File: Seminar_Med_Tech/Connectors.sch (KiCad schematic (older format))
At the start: 12 parts, among them J1 TP10, J2 CONN_02X10, J3 TP7, J4 CONN_02X10

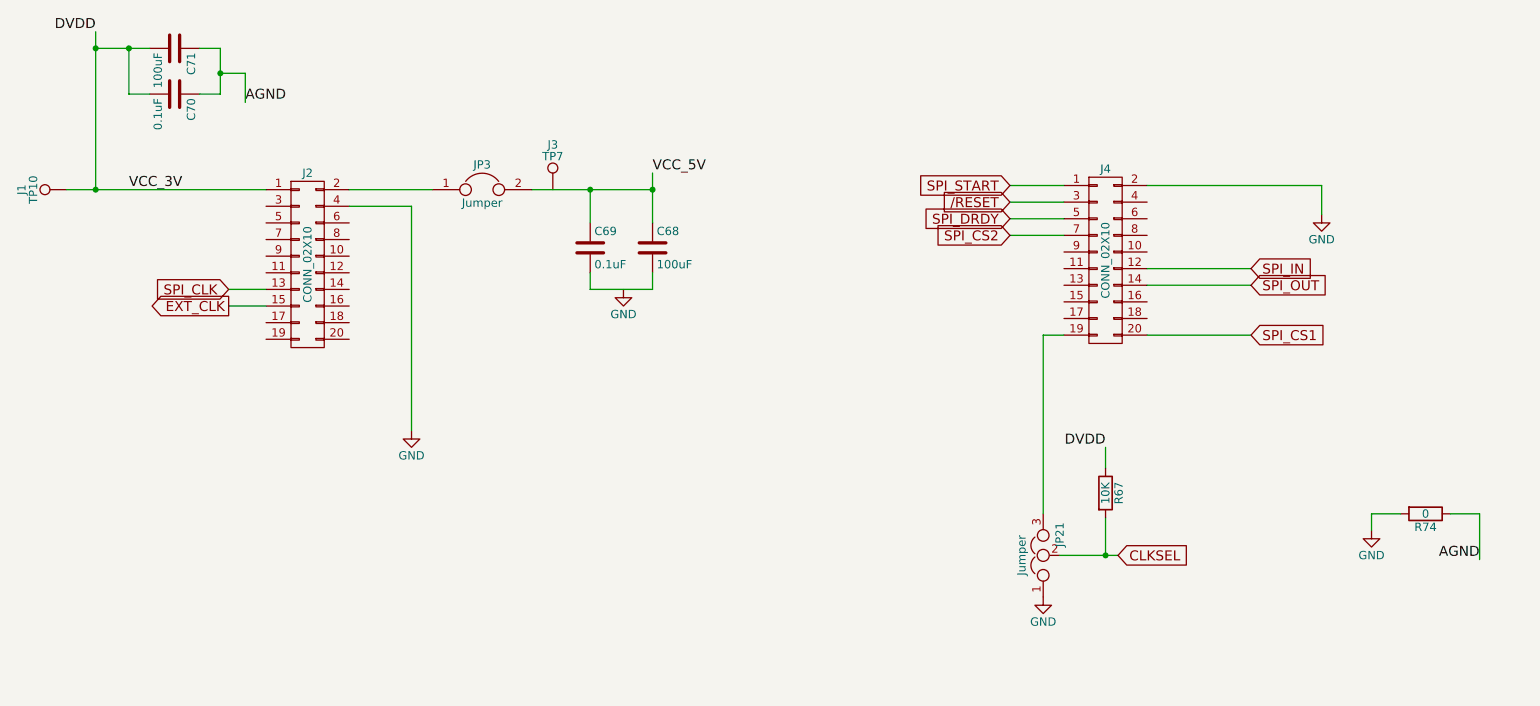
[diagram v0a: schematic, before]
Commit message: Changed labels in ADC1298_ECG_FE
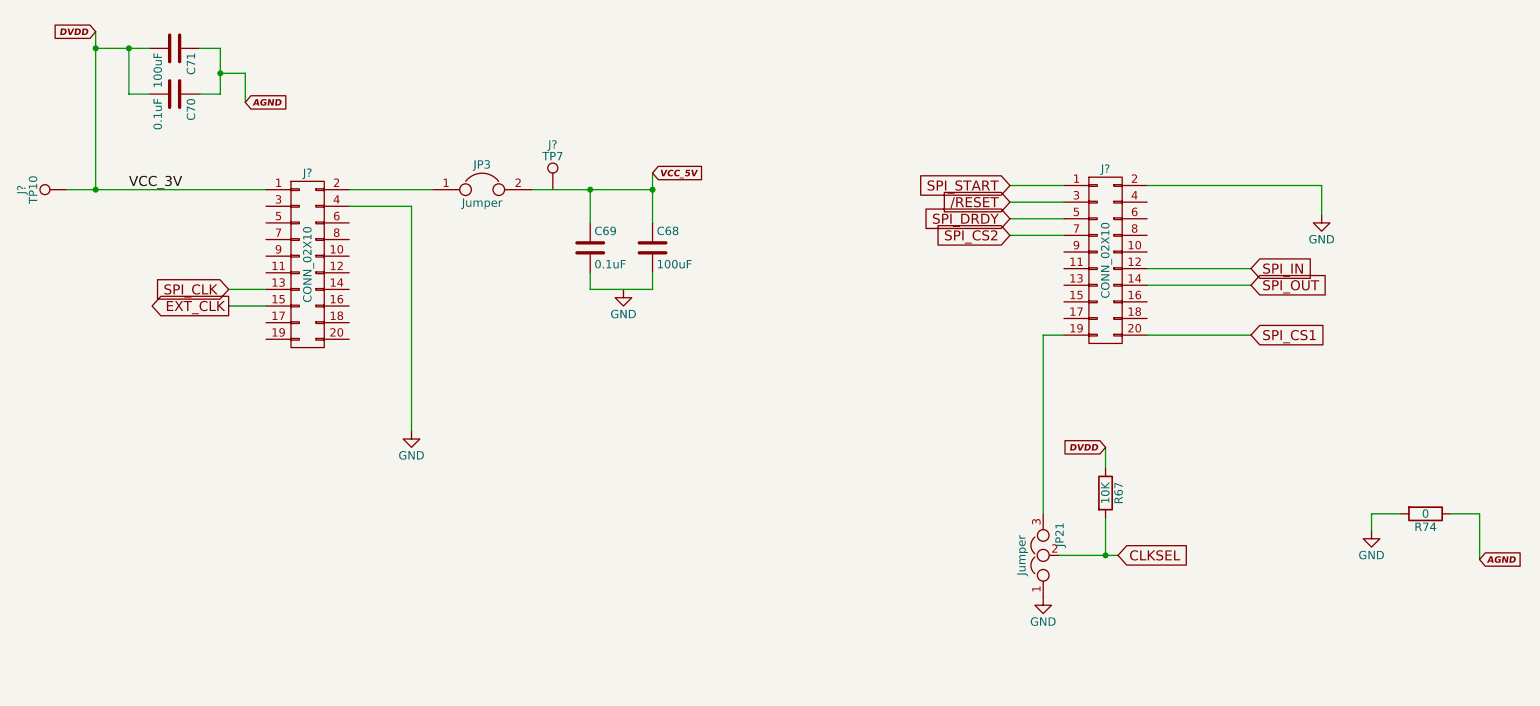
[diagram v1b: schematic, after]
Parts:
- C68, C69, C70, C71: footprint Capacitors_SMD:C_1206_HandSoldering -> (none)
- J?: renamed from J2; footprint Pin_Headers:Pin_Header_Angled_2x10_Pitch2.54mm -> (none)
- J?: renamed from J4; footprint Pin_Headers:Pin_Header_Angled_2x10_Pitch2.54mm -> (none)
- J?: renamed from J1; footprint Measurement_Points:Test_Point -> (none)
- J?: renamed from J3; footprint Measurement_Points:Test_Point -> (none)
- JP21: footprint jumper:jumper1x3 -> (none)
- JP3: footprint jumper:Jumper1x2 -> (none)
- R67, R74: footprint Resistors_SMD:R_0805_HandSoldering -> (none)
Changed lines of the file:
@@
 $EndDescr
 $Comp
-L CONN_02X10 J2
+L CONN_02X10 J?
 U 1 1 593ACF11
 P 2800 4000
-F 0 "J2" H 2800 4550 50  0000 C CNN
+F 0 "J?" H 2800 4550 50  0000 C CNN
 F 1 "CONN_02X10" V 2800 4000 50  0000 C CNN
-F 2 "Pin_Headers:Pin_Header_Angled_2x10_Pitch2.54mm" H 2800 2800 50  0001 C CNN
+F 2 "" H 2800 2800 50  0001 C CNN
 F 3 "" H 2800 2800 50  0001 C CNN
 	1    2800 4000
@@
 $EndComp
 $Comp
-L CONN_02X10 J4
+L CONN_02X10 J?
 U 1 1 593AD152
 P 7600 3975
-F 0 "J4" H 7600 4525 50  0000 C CNN
+F 0 "J?" H 7600 4525 50  0000 C CNN
 F 1 "CONN_02X10" V 7600 3975 50  0000 C CNN
-F 2 "Pin_Headers:Pin_Header_Angled_2x10_Pitch2.54mm" H 7600 2775 50  0001 C CNN
+F 2 "" H 7600 2775 50  0001 C CNN
 F 3 "" H 7600 2775 50  0001 C CNN
 	1    7600 3975
@@
 F 0 "JP21" H 7275 5650 50  0000 L CNN
 F 1 "Jumper" H 7225 5850 50  0000 C BNN
-F 2 "jumper:jumper1x3" H 7225 5750 50  0001 C CNN
+F 2 "" H 7225 5750 50  0001 C CNN
 F 3 "" H 7225 5750 50  0001 C CNN
 	1    7225 5750
@@
 F 0 "R67" V 7680 5375 50  0000 C CNN
 F 1 "10K" V 7600 5375 50  0000 C CNN
-F 2 "Resistors_SMD:R_0805_HandSoldering" V 7530 5375 50  0001 C CNN
+F 2 "" V 7530 5375 50  0001 C CNN
 F 3 "" H 7600 5375 50  0001 C CNN
 	1    7600 5375
 	1    0    0    -1
 $EndComp
-Text Label 7600 5100 2    60   ~ 0
-DVDD
-$Comp
-L GND #PWR01
+$Comp
+L GND #PWR?
 U 1 1 593AE084
 P 7225 6000
-F 0 "#PWR01" H 7225 5750 50  0001 C CNN
+F 0 "#PWR?" H 7225 5750 50  0001 C CNN
 F 1 "GND" H 7225 5850 50  0000 C CNN
 F 2 "" H 7225 6000 50  0001 C CNN
@@
 $EndComp
 $Comp
-L GND #PWR02
+L GND #PWR?
 U 1 1 593AE114
 P 3425 5000
-F 0 "#PWR02" H 3425 4750 50  0001 C CNN
+F 0 "#PWR?" H 3425 4750 50  0001 C CNN
 F 1 "GND" H 3425 4850 50  0000 C CNN
 F 2 "" H 3425 5000 50  0001 C CNN
@@
 $EndComp
 $Comp
-L GND #PWR03
+L GND #PWR?
 U 1 1 593AE149
 P 8900 3700
-F 0 "#PWR03" H 8900 3450 50  0001 C CNN
+F 0 "#PWR?" H 8900 3450 50  0001 C CNN
 F 1 "GND" H 8900 3550 50  0000 C CNN
 F 2 "" H 8900 3700 50  0001 C CNN
@@
 SPI_CS1
 $Comp
-L GND #PWR04
+L GND #PWR?
 U 1 1 593E72B3
 P 9200 5600
-F 0 "#PWR04" H 9200 5350 50  0001 C CNN
+F 0 "#PWR?" H 9200 5350 50  0001 C CNN
 F 1 "GND" H 9200 5450 50  0000 C CNN
 F 2 "" H 9200 5600 50  0001 C CNN
@@
 F 0 "R74" V 9605 5500 50  0000 C CNN
 F 1 "0" V 9525 5500 50  0000 C CNN
-F 2 "Resistors_SMD:R_0805_HandSoldering" V 9455 5500 50  0001 C CNN
+F 2 "" V 9455 5500 50  0001 C CNN
 F 3 "" H 9525 5500 50  0001 C CNN
 	1    9525 5500
 	0    1    1    0
 $EndComp
-Text Label 9850 5775 2    60   ~ 0
-AGND
-$Comp
-L TEST_1P J1
+$Comp
+L TEST_1P J?
 U 1 1 593E7E55
 P 1350 3550
-F 0 "J1" H 1350 3820 50  0000 C CNN
+F 0 "J?" H 1350 3820 50  0000 C CNN
 F 1 "TP10" H 1350 3750 50  0000 C CNN
-F 2 "Measurement_Points:Test_Point" H 1550 3550 50  0001 C CNN
+F 2 "" H 1550 3550 50  0001 C CNN
 F 3 "" H 1550 3550 50  0001 C CNN
 	1    1350 3550
 	0    -1   -1   0
 $EndComp
-Text Label 1525 2600 2    60   ~ 0
-DVDD
 $Comp
 L C C71
@@
 F 0 "C71" H 2025 2800 50  0000 L CNN
 F 1 "100uF" H 2025 2600 50  0000 L CNN
-F 2 "Capacitors_SMD:C_1206_HandSoldering" H 2038 2550 50  0001 C CNN
+F 2 "" H 2038 2550 50  0001 C CNN
 F 3 "" H 2000 2700 50  0001 C CNN
 	1    2000 2700
@@
 F 0 "C70" H 2025 3075 50  0000 L CNN
 F 1 "0.1uF" H 2025 2875 50  0000 L CNN
-F 2 "Capacitors_SMD:C_1206_HandSoldering" H 2038 2825 50  0001 C CNN
+F 2 "" H 2038 2825 50  0001 C CNN
 F 3 "" H 2000 2975 50  0001 C CNN
 	1    2000 2975
 	0    1    1    0
 $EndComp
-Text Label 2425 3025 0    60   ~ 0
-AGND
 $Comp
 L Jumper JP3
@@
 F 0 "JP3" H 3850 3700 50  0000 C CNN
 F 1 "Jumper" H 3850 3470 50  0000 C CNN
-F 2 "jumper:Jumper1x2" H 3850 3550 50  0001 C CNN
+F 2 "" H 3850 3550 50  0001 C CNN
 F 3 "" H 3850 3550 50  0001 C CNN
 	1    3850 3550
@@
 $EndComp
 $Comp
-L TEST_1P J3
+L TEST_1P J?
 U 1 1 593E9035
 P 4275 3550
-F 0 "J3" H 4275 3820 50  0000 C CNN
+F 0 "J?" H 4275 3820 50  0000 C CNN
 F 1 "TP7" H 4275 3750 50  0000 C CNN
-F 2 "Measurement_Points:Test_Point" H 4475 3550 50  0001 C CNN
+F 2 "" H 4475 3550 50  0001 C CNN
 F 3 "" H 4475 3550 50  0001 C CNN
 	1    4275 3550
@@
 F 0 "C69" H 4525 4000 50  0000 L CNN
 F 1 "0.1uF" H 4525 3800 50  0000 L CNN
-F 2 "Capacitors_SMD:C_1206_HandSoldering" H 4538 3750 50  0001 C CNN
+F 2 "" H 4538 3750 50  0001 C CNN
 F 3 "" H 4500 3900 50  0001 C CNN
 	1    4500 3900
@@
 F 0 "C68" H 4900 4000 50  0000 L CNN
 F 1 "100uF" H 4900 3800 50  0000 L CNN
-F 2 "Capacitors_SMD:C_1206_HandSoldering" H 4913 3750 50  0001 C CNN
+F 2 "" H 4913 3750 50  0001 C CNN
 F 3 "" H 4875 3900 50  0001 C CNN
 	1    4875 3900
@@
 $EndComp
 $Comp
-L GND #PWR05
+L GND #PWR?
 U 1 1 593E9316
 P 4700 4150
-F 0 "#PWR05" H 4700 3900 50  0001 C CNN
+F 0 "#PWR?" H 4700 3900 50  0001 C CNN
 F 1 "GND" H 4700 4000 50  0000 C CNN
 F 2 "" H 4700 4150 50  0001 C CNN
@@
 Text Label 1725 3550 0    60   ~ 0
 VCC_3V
-Text Label 4875 3450 0    60   ~ 0
-VCC_5V
 Wire Wire Line
 	2550 4150 2325 4150
@@
 	4875 4150 4875 4050
 Connection ~ 4875 3550
+Text GLabel 1525 2600 0    39   Input Italic 8
+DVDD
+Text GLabel 2425 3025 2    39   Input Italic 8
+AGND
+Text GLabel 4875 3450 2    39   Input Italic 8
+VCC_5V
+Text GLabel 7600 5100 0    39   Input Italic 8
+DVDD
+Text GLabel 9850 5775 2    39   Input Italic 8
+AGND
 $EndSCHEMATC

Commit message: Update
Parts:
- added J2: CONN_01X10, symbol CONN_01X10
- JP21: value Jumper -> Jumper_NC_Dual
- TP10: renamed from J?; value TP10 -> TEST
- TP7: renamed from J?; value TP7 -> TEST
- gave numbers to parts that had none: 2
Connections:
- net VCC_5V: now also TP7.1
- net GPIO22: now reaches J3.17 (P17)
- net GPIO12: now reaches J3.5 (P5)
- net GPIO21: now reaches J3.7 (P7)
- net GPIO11: now reaches J3.9 (P9)
- net I/O_2: now reaches J5.11 (P11)
- net I/O_2: now also J2.2 (P2)
- net I/O_3: now reaches J5.13 (P13)
- net I/O_3: now also J2.3 (P3)
- net I/O_4: now reaches J5.15 (P15)
- net I/O_4: now also J2.4 (P4)
- net I/O_5: now reaches J5.17 (P17)
- net I/O_5: now also J2.5 (P5)
- net I/O_6: now reaches J5.4 (P4)
- net I/O_6: now also J2.6 (P6)
- net I/O_7: now reaches J5.6 (P6)
- net I/O_7: now also J2.7 (P7)
- net I/O_8: now reaches J5.8 (P8)
- net I/O_8: now also J2.8 (P8)
- net I/O_1: now reaches J5.9 (P9)
- net I/O_1: now also J2.1 (P1)
- no-connect marks 0 -> 14
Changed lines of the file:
@@
 $EndDescr
 $Comp
-L CONN_02X10 J?
+L CONN_02X10 J3
 U 1 1 593ACF11
 P 2800 4000
-F 0 "J?" H 2800 4550 50  0000 C CNN
+F 0 "J3" H 2800 4550 50  0000 C CNN
 F 1 "CONN_02X10" V 2800 4000 50  0000 C CNN
 F 2 "" H 2800 2800 50  0001 C CNN
@@
 $EndComp
 $Comp
-L CONN_02X10 J?
+L CONN_02X10 J5
 U 1 1 593AD152
 P 7600 3975
-F 0 "J?" H 7600 4525 50  0000 C CNN
+F 0 "J5" H 7600 4525 50  0000 C CNN
 F 1 "CONN_02X10" V 7600 3975 50  0000 C CNN
 F 2 "" H 7600 2775 50  0001 C CNN
@@
 P 7225 5750
 F 0 "JP21" H 7275 5650 50  0000 L CNN
-F 1 "Jumper" H 7225 5850 50  0000 C BNN
+F 1 "Jumper_NC_Dual" H 7225 5850 50  0000 C BNN
 F 2 "" H 7225 5750 50  0001 C CNN
 F 3 "" H 7225 5750 50  0001 C CNN
@@
 $EndComp
 $Comp
-L GND #PWR?
+L GND #PWR03
 U 1 1 593AE084
 P 7225 6000
-F 0 "#PWR?" H 7225 5750 50  0001 C CNN
+F 0 "#PWR03" H 7225 5750 50  0001 C CNN
 F 1 "GND" H 7225 5850 50  0000 C CNN
 F 2 "" H 7225 6000 50  0001 C CNN
@@
 $EndComp
 $Comp
-L GND #PWR?
+L GND #PWR04
 U 1 1 593AE114
-P 3425 5000
-F 0 "#PWR?" H 3425 4750 50  0001 C CNN
-F 1 "GND" H 3425 4850 50  0000 C CNN
-F 2 "" H 3425 5000 50  0001 C CNN
-F 3 "" H 3425 5000 50  0001 C CNN
-	1    3425 5000
-	1    0    0    -1
-$EndComp
-$Comp
-L GND #PWR?
+P 3675 5000
+F 0 "#PWR04" H 3675 4750 50  0001 C CNN
+F 1 "GND" H 3675 4850 50  0000 C CNN
+F 2 "" H 3675 5000 50  0001 C CNN
+F 3 "" H 3675 5000 50  0001 C CNN
+	1    3675 5000
+	1    0    0    -1
+$EndComp
+$Comp
+L GND #PWR05
 U 1 1 593AE149
-P 8900 3700
-F 0 "#PWR?" H 8900 3450 50  0001 C CNN
-F 1 "GND" H 8900 3550 50  0000 C CNN
-F 2 "" H 8900 3700 50  0001 C CNN
-F 3 "" H 8900 3700 50  0001 C CNN
-	1    8900 3700
+P 9375 3700
+F 0 "#PWR05" H 9375 3450 50  0001 C CNN
+F 1 "GND" H 9375 3550 50  0000 C CNN
+F 2 "" H 9375 3700 50  0001 C CNN
+F 3 "" H 9375 3700 50  0001 C CNN
+	1    9375 3700
 	1    0    0    -1
 $EndComp
@@
 SPI_CS1
 $Comp
-L GND #PWR?
+L GND #PWR06
 U 1 1 593E72B3
 P 9200 5600
-F 0 "#PWR?" H 9200 5350 50  0001 C CNN
+F 0 "#PWR06" H 9200 5350 50  0001 C CNN
 F 1 "GND" H 9200 5450 50  0000 C CNN
 F 2 "" H 9200 5600 50  0001 C CNN
@@
 $EndComp
 $Comp
-L TEST_1P J?
+L TEST_1P TP10
 U 1 1 593E7E55
 P 1350 3550
-F 0 "J?" H 1350 3820 50  0000 C CNN
-F 1 "TP10" H 1350 3750 50  0000 C CNN
+F 0 "TP10" H 1350 3820 50  0000 C CNN
+F 1 "TEST" H 1350 3750 50  0000 C CNN
 F 2 "" H 1550 3550 50  0001 C CNN
 F 3 "" H 1550 3550 50  0001 C CNN
@@
 $EndComp
 $Comp
-L TEST_1P J?
+L TEST_1P TP7
 U 1 1 593E9035
 P 4275 3550
-F 0 "J?" H 4275 3820 50  0000 C CNN
-F 1 "TP7" H 4275 3750 50  0000 C CNN
+F 0 "TP7" H 4275 3820 50  0000 C CNN
+F 1 "TEST" H 4275 3750 50  0000 C CNN
 F 2 "" H 4475 3550 50  0001 C CNN
 F 3 "" H 4475 3550 50  0001 C CNN
@@
 $EndComp
 $Comp
-L GND #PWR?
+L GND #PWR07
 U 1 1 593E9316
 P 4700 4150
-F 0 "#PWR?" H 4700 3900 50  0001 C CNN
+F 0 "#PWR07" H 4700 3900 50  0001 C CNN
 F 1 "GND" H 4700 4000 50  0000 C CNN
 F 2 "" H 4700 4150 50  0001 C CNN
@@
 Text Label 1725 3550 0    60   ~ 0
 VCC_3V
-Wire Wire Line
-	2550 4150 2325 4150
-Wire Wire Line
-	8475 4025 7850 4025
-Wire Wire Line
-	7850 4125 8475 4125
-Wire Wire Line
-	7025 3825 7350 3825
-Wire Wire Line
-	7350 3525 7025 3525
-Wire Wire Line
-	7350 3725 7025 3725
-Wire Wire Line
-	7025 3625 7350 3625
-Wire Wire Line
-	2325 4250 2550 4250
-Wire Wire Line
-	7325 5750 7675 5750
-Wire Wire Line
-	7600 5525 7600 5750
-Connection ~ 7600 5750
-Wire Wire Line
-	7600 5225 7600 5100
-Wire Wire Line
-	3050 3650 3425 3650
-Wire Wire Line
-	3425 3650 3425 5000
-Wire Wire Line
-	7850 3525 8900 3525
-Wire Wire Line
-	8900 3525 8900 3700
-Wire Wire Line
-	7850 4425 8475 4425
-Wire Wire Line
-	7350 4425 7225 4425
-Wire Wire Line
-	7225 4425 7225 5500
-Wire Wire Line
-	9375 5500 9200 5500
-Wire Wire Line
-	9200 5500 9200 5600
-Wire Wire Line
-	9675 5500 9850 5500
-Wire Wire Line
-	9850 5500 9850 5775
-Wire Wire Line
-	1350 3550 2550 3550
-Wire Wire Line
-	1525 2600 1525 3550
-Connection ~ 1525 3550
-Wire Wire Line
-	1525 2700 1850 2700
-Connection ~ 1525 2700
-Wire Wire Line
-	1725 2700 1725 2975
-Wire Wire Line
-	1725 2975 1850 2975
-Connection ~ 1725 2700
-Wire Wire Line
-	2150 2700 2275 2700
-Wire Wire Line
-	2275 2700 2275 2975
-Wire Wire Line
-	2275 2975 2150 2975
-Wire Wire Line
-	2275 2850 2425 2850
-Wire Wire Line
-	2425 2850 2425 3025
-Connection ~ 2275 2850
-Wire Wire Line
-	3050 3550 3550 3550
-Wire Wire Line
-	4150 3550 4875 3550
-Wire Wire Line
-	4875 3450 4875 3750
-Wire Wire Line
-	4500 3750 4500 3550
-Connection ~ 4500 3550
-Wire Wire Line
-	4500 4050 4500 4150
-Wire Wire Line
-	4500 4150 4875 4150
-Wire Wire Line
-	4875 4150 4875 4050
-Connection ~ 4875 3550
 Text GLabel 1525 2600 0    39   Input Italic 8
 DVDD
@@
 Text GLabel 9850 5775 2    39   Input Italic 8
 AGND
+Text GLabel 7025 3925 0    60   Input ~ 0
+I/O_1
+Text GLabel 7025 4025 0    60   Input ~ 0
+I/O_2
+Text GLabel 7025 4125 0    60   Input ~ 0
+I/O_3
+Text GLabel 7025 4225 0    60   Input ~ 0
+I/O_4
+Text GLabel 7025 4325 0    60   Input ~ 0
+I/O_5
+Text GLabel 8475 3825 2    60   Input ~ 0
+I/O_8
+Text GLabel 8475 3725 2    60   Input ~ 0
+I/O_7
+Text GLabel 8475 3625 2    60   Input ~ 0
+I/O_6
+Wire Wire Line
+	2550 4150 2325 4150
+Wire Wire Line
+	8475 4025 7850 4025
+Wire Wire Line
+	7850 4125 8475 4125
+Wire Wire Line
+	7025 3825 7350 3825
+Wire Wire Line
+	7350 3525 7025 3525
+Wire Wire Line
+	7350 3725 7025 3725
+Wire Wire Line
+	7025 3625 7350 3625
+Wire Wire Line
+	2325 4250 2550 4250
+Wire Wire Line
+	7325 5750 7675 5750
+Wire Wire Line
+	7600 5525 7600 5750
+Connection ~ 7600 5750
+Wire Wire Line
+	7600 5225 7600 5100
+Wire Wire Line
+	3050 3650 3675 3650
+Wire Wire Line
+	3675 3650 3675 5000
+Wire Wire Line
+	7850 3525 9375 3525
+Wire Wire Line
+	9375 3525 9375 3700
+Wire Wire Line
+	7850 4425 8475 4425
+Wire Wire Line
+	7350 4425 7225 4425
+Wire Wire Line
+	7225 4425 7225 5500
+Wire Wire Line
+	9375 5500 9200 5500
+Wire Wire Line
+	9200 5500 9200 5600
+Wire Wire Line
+	9675 5500 9850 5500
+Wire Wire Line
+	9850 5500 9850 5775
+Wire Wire Line
+	1350 3550 2550 3550
+Wire Wire Line
+	1525 2600 1525 3550
+Connection ~ 1525 3550
+Wire Wire Line
+	1525 2700 1850 2700
+Connection ~ 1525 2700
+Wire Wire Line
+	1725 2700 1725 2975
+Wire Wire Line
+	1725 2975 1850 2975
+Connection ~ 1725 2700
+Wire Wire Line
+	2150 2700 2275 2700
+Wire Wire Line
+	2275 2700 2275 2975
+Wire Wire Line
+	2275 2975 2150 2975
+Wire Wire Line
+	2275 2850 2425 2850
+Wire Wire Line
+	2425 2850 2425 3025
+Connection ~ 2275 2850
+Wire Wire Line
+	3050 3550 3550 3550
+Wire Wire Line
+	4150 3550 4875 3550
+Wire Wire Line
+	4875 3450 4875 3750
+Wire Wire Line
+	4500 3750 4500 3550
+Wire Wire Line
+	4500 4050 4500 4150
+Wire Wire Line
+	4500 4150 4875 4150
+Wire Wire Line
+	4875 4150 4875 4050
+Connection ~ 4875 3550
+Wire Wire Line
+	7350 3925 7025 3925
+Wire Wire Line
+	7025 4025 7350 4025
+Wire Wire Line
+	7350 4125 7025 4125
+Wire Wire Line
+	7025 4225 7350 4225
+Wire Wire Line
+	7025 4325 7350 4325
+Wire Wire Line
+	8475 3625 7850 3625
+Wire Wire Line
+	7850 3725 8475 3725
+Wire Wire Line
+	7850 3825 8475 3825
+Text GLabel 2325 3950 0    60   Input ~ 0
+GPIO11
+Wire Wire Line
+	2550 3950 2325 3950
+Text GLabel 2325 3750 0    60   Input ~ 0
+GPIO12
+Text GLabel 2325 3850 0    60   Input ~ 0
+GPIO21
+Text GLabel 2325 4350 0    60   Input ~ 0
+GPIO22
+Wire Wire Line
+	2325 3750 2550 3750
+Wire Wire Line
+	2550 3850 2325 3850
+Wire Wire Line
+	2325 4350 2550 4350
+$Comp
+L CONN_01X10 J2
+U 1 1 5962D12A
+P 4200 6425
+F 0 "J2" H 4200 6975 50  0000 C CNN
+F 1 "CONN_01X10" V 4300 6425 50  0000 C CNN
+F 2 "" H 4200 6425 50  0001 C CNN
+F 3 "" H 4200 6425 50  0001 C CNN
+	1    4200 6425
+	0    1    1    0
+$EndComp
+Text GLabel 4650 6225 1    60   Input ~ 0
+I/O_1
+Text GLabel 4550 6225 1    60   Input ~ 0
+I/O_2
+Text GLabel 4450 6225 1    60   Input ~ 0
+I/O_3
+Text GLabel 4350 6225 1    60   Input ~ 0
+I/O_4
+Text GLabel 4250 6225 1    60   Input ~ 0
+I/O_5
+Text GLabel 4150 6225 1    60   Input ~ 0
+I/O_6
+Text GLabel 4050 6225 1    60   Input ~ 0
+I/O_7
+Text GLabel 3950 6225 1    60   Input ~ 0
+I/O_8
+NoConn ~ 3050 3750
+NoConn ~ 3050 3850
+NoConn ~ 3050 3950
+NoConn ~ 3050 4050
+NoConn ~ 3050 4150
+NoConn ~ 3050 4275
+NoConn ~ 3050 4350
+NoConn ~ 3050 4450
+NoConn ~ 2550 4450
+NoConn ~ 2550 4050
+NoConn ~ 2550 3650
+NoConn ~ 7850 3925
+NoConn ~ 7850 4225
+NoConn ~ 7850 4325
+Connection ~ 4500 3550
+Connection ~ 4275 3550
 $EndSCHEMATC
